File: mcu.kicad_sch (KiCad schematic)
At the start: 35 parts, among them J2 SWD, J3 SWC, U1 NRF52840-QIAA-R, Y1 ECS-.327-9-34B-TR, Y2 XRCGB32M000F1S2KR0

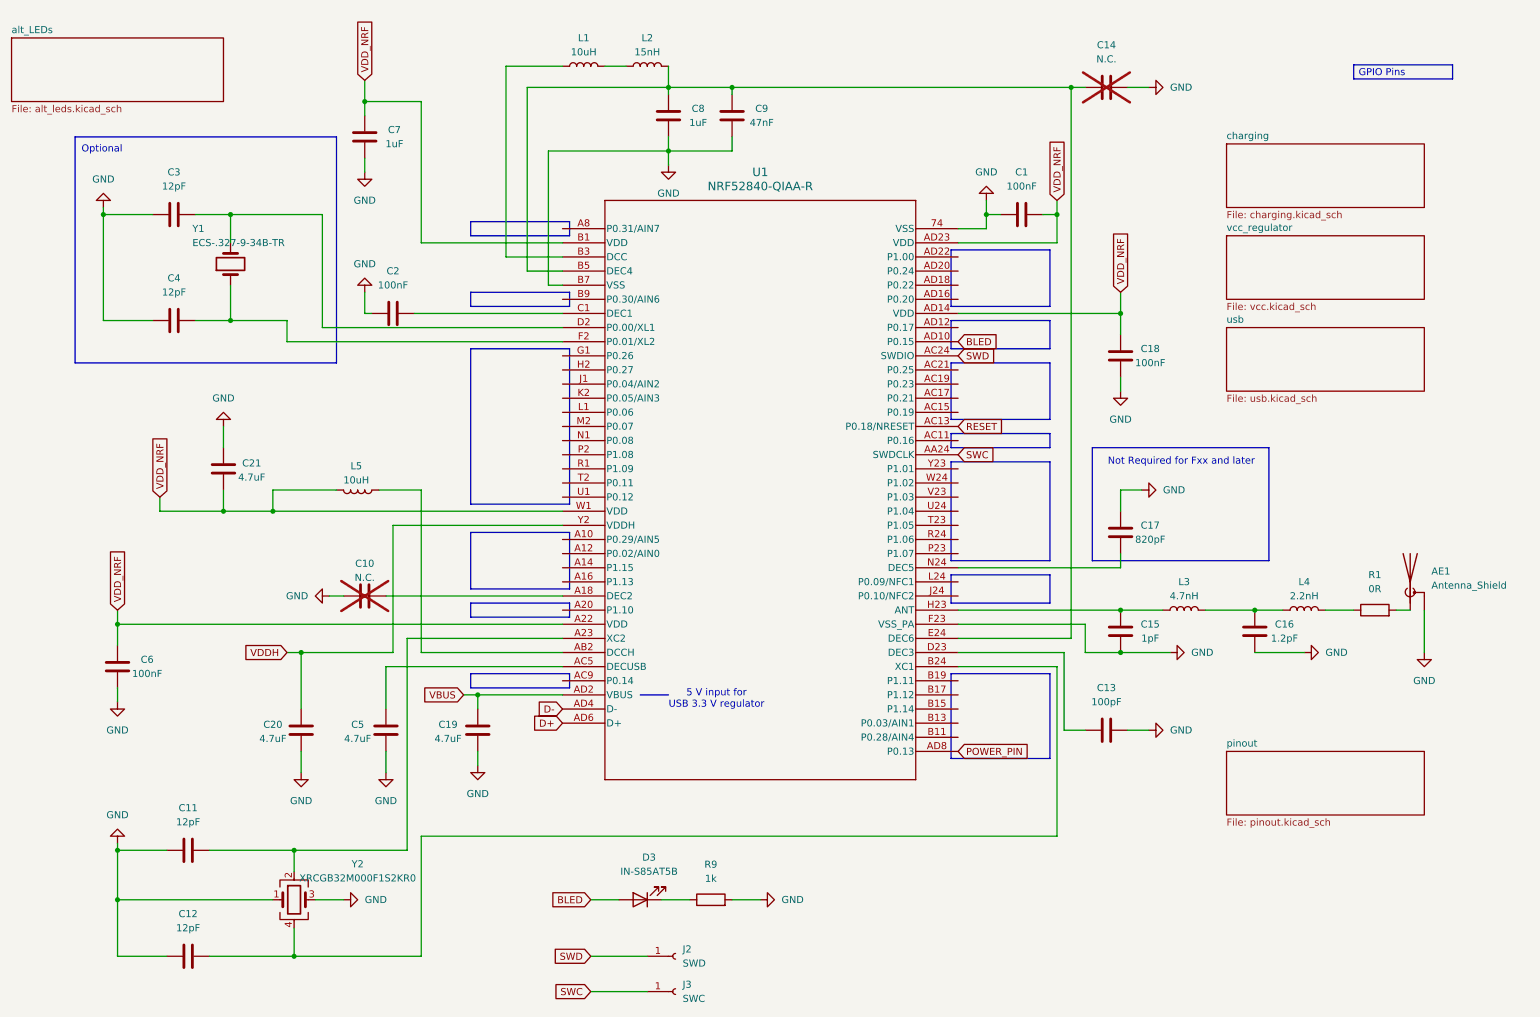
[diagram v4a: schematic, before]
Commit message: Connected GPIO
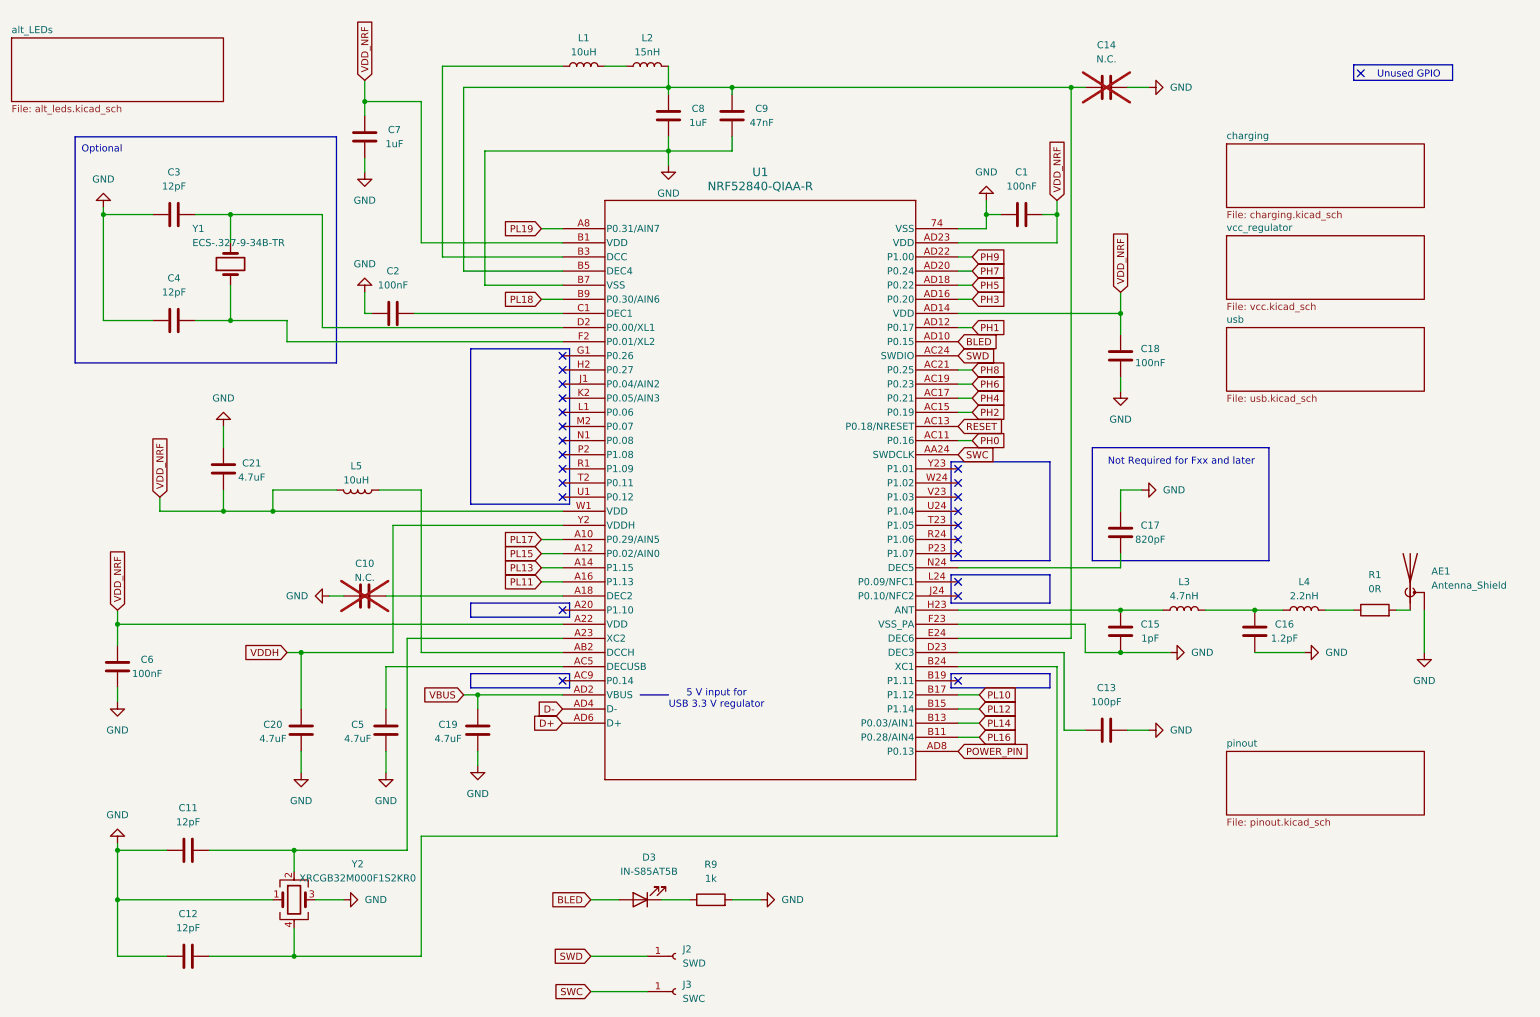
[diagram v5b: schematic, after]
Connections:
- net PL17: now reaches U1.A10 (P0.29/AIN5)
- net PL15: now reaches U1.A12 (P0.02/AIN0)
- net PL13: now reaches U1.A14 (P1.15)
- net PL11: now reaches U1.A16 (P1.13)
- net PL19: now reaches U1.A8 (P0.31/AIN7)
- net PH0: now reaches U1.AC11 (P0.16)
- net PH2: now reaches U1.AC15 (P0.19)
- net PH4: now reaches U1.AC17 (P0.21)
- net PH6: now reaches U1.AC19 (P0.23)
- net PH8: now reaches U1.AC21 (P0.25)
- net PH1: now reaches U1.AD12 (P0.17)
- net PH3: now reaches U1.AD16 (P0.20)
- net PH5: now reaches U1.AD18 (P0.22)
- net PH7: now reaches U1.AD20 (P0.24)
- net PH9: now reaches U1.AD22 (P1.00)
- net PL16: now reaches U1.B11 (P0.28/AIN4)
- net PL14: now reaches U1.B13 (P0.03/AIN1)
- net PL12: now reaches U1.B15 (P1.14)
- net PL10: now reaches U1.B17 (P1.12)
- net PL18: now reaches U1.B9 (P0.30/AIN6)
- no-connect marks 0 -> 24
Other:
- note added: "Unused GPIO"
- note removed: "GPIO Pins"

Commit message: Placed Components and started routing
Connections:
- net GND: now also Y2.2, Y2.4; no longer Y2.1, Y2.3
- net at C12.1, U1.B24 (XC1): now also Y2.1; no longer Y2.4
- net at C11.1, U1.A23 (XC2): now also Y2.3; no longer Y2.2
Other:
- moved on the sheet: Y2
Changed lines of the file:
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@@
 	)
 	(junction
-		(at 69.85 163.83)
+		(at 71.12 128.27)
 		(diameter 0)
 		(color 0 0 0 0)
@@
 	)
 	(junction
-		(at 71.12 128.27)
+		(at 38.1 163.83)
 		(diameter 0)
 		(color 0 0 0 0)
 	)
 	(junction
-		(at 38.1 163.83)
+		(at 58.42 49.53)
 		(diameter 0)
 		(color 0 0 0 0)
 	)
 	(junction
-		(at 58.42 49.53)
+		(at 57.15 102.87)
 		(diameter 0)
 		(color 0 0 0 0)
 	)
 	(junction
-		(at 38.1 172.72)
+		(at 148.59 26.67)
 		(diameter 0)
 		(color 0 0 0 0)
 	)
 	(junction
-		(at 57.15 102.87)
+		(at 38.1 172.72)
 		(diameter 0)
 		(color 0 0 0 0)
 	)
 	(junction
-		(at 148.59 26.67)
+		(at 69.85 163.83)
 		(diameter 0)
 		(color 0 0 0 0)
@@
 	(wire
 		(pts
+			(xy 69.85 163.83) (xy 69.85 168.91)
+		)
+		(stroke
+			(width 0)
+			(type default)
+		)
+	)
+	(wire
+		(pts
 			(xy 148.59 26.67) (xy 137.16 26.67)
 		)
@@
 	(wire
 		(pts
-			(xy 267.97 120.65) (xy 270.51 120.65)
+			(xy 69.85 182.88) (xy 92.71 182.88)
 		)
 		(stroke
@@
 	(wire
 		(pts
-			(xy 242.57 128.27) (xy 251.46 128.27)
+			(xy 267.97 120.65) (xy 270.51 120.65)
 		)
 		(stroke
@@
 	(wire
 		(pts
-			(xy 38.1 172.72) (xy 66.04 172.72)
+			(xy 242.57 128.27) (xy 251.46 128.27)
 		)
 		(stroke
@@
 	(wire
 		(pts
-			(xy 69.85 163.83) (xy 90.17 163.83)
+			(xy 96.52 22.86) (xy 118.11 22.86)
 		)
 		(stroke
@@
 	(wire
 		(pts
-			(xy 96.52 22.86) (xy 118.11 22.86)
+			(xy 189.23 59.69) (xy 191.77 59.69)
 		)
 		(stroke
@@
 	(wire
 		(pts
-			(xy 189.23 59.69) (xy 191.77 59.69)
+			(xy 69.85 176.53) (xy 69.85 182.88)
 		)
 		(stroke
@@
 	(wire
 		(pts
+			(xy 38.1 172.72) (xy 64.77 172.72)
+		)
+		(stroke
+			(width 0)
+			(type default)
+		)
+	)
+	(wire
+		(pts
 			(xy 38.1 163.83) (xy 38.1 162.56)
 		)
@@
 	(wire
 		(pts
+			(xy 38.1 172.72) (xy 38.1 182.88)
+		)
+		(stroke
+			(width 0)
+			(type default)
+		)
+	)
+	(wire
+		(pts
 			(xy 118.11 54.61) (xy 92.71 54.61)
 		)
@@
 	(wire
 		(pts
-			(xy 54.61 182.88) (xy 69.85 182.88)
-		)
-		(stroke
-			(width 0)
-			(type default)
-		)
-	)
-	(wire
-		(pts
 			(xy 148.59 172.72) (xy 153.67 172.72)
 		)
@@
 	(wire
 		(pts
-			(xy 38.1 172.72) (xy 38.1 182.88)
-		)
-		(stroke
-			(width 0)
-			(type default)
-		)
-	)
-	(wire
-		(pts
 			(xy 74.93 49.53) (xy 58.42 49.53)
 		)
@@
 	(wire
 		(pts
-			(xy 69.85 177.8) (xy 69.85 182.88)
-		)
-		(stroke
-			(width 0)
-			(type default)
-		)
-	)
-	(wire
-		(pts
 			(xy 74.93 69.85) (xy 74.93 49.53)
 		)
@@
 	(wire
 		(pts
+			(xy 74.93 172.72) (xy 78.74 172.72)
+		)
+		(stroke
+			(width 0)
+			(type default)
+		)
+	)
+	(wire
+		(pts
 			(xy 118.11 128.27) (xy 92.71 128.27)
 		)
@@
 	(wire
 		(pts
-			(xy 73.66 172.72) (xy 78.74 172.72)
-		)
-		(stroke
-			(width 0)
-			(type default)
-		)
-	)
-	(wire
-		(pts
 			(xy 38.1 120.65) (xy 38.1 123.19)
 		)
@@
 	(wire
 		(pts
-			(xy 69.85 163.83) (xy 69.85 167.64)
-		)
-		(stroke
-			(width 0)
-			(type default)
-		)
-	)
-	(wire
-		(pts
 			(xy 209.55 26.67) (xy 148.59 26.67)
 		)
@@
 	(wire
 		(pts
-			(xy 69.85 182.88) (xy 92.71 182.88)
+			(xy 54.61 182.88) (xy 69.85 182.88)
 		)
 		(stroke
@@
 		)
 	)
+	(wire
+		(pts
+			(xy 69.85 163.83) (xy 90.17 163.83)
+		)
+		(stroke
+			(width 0)
+			(type default)
+		)
+	)
 	(global_label "PL13"
 		(shape input)
@@
 	(symbol
 		(lib_id "Device:Crystal_GND24")
-		(at 69.85 172.72 0)
+		(at 69.85 172.72 90)
 		(unit 1)
 		(exclude_from_sim no)
@@
 		(fields_autoplaced yes)
 		(property "Reference" "Y2"
-			(at 81.28 166.2998 0)
+			(at 86.36 167.7668 90)
 			(effects
 				(font
@@
 		)
 		(property "Value" "XRCGB32M000F1S2KR0"
-			(at 81.28 168.8398 0)
+			(at 86.36 170.3068 90)
 			(effects
 				(font

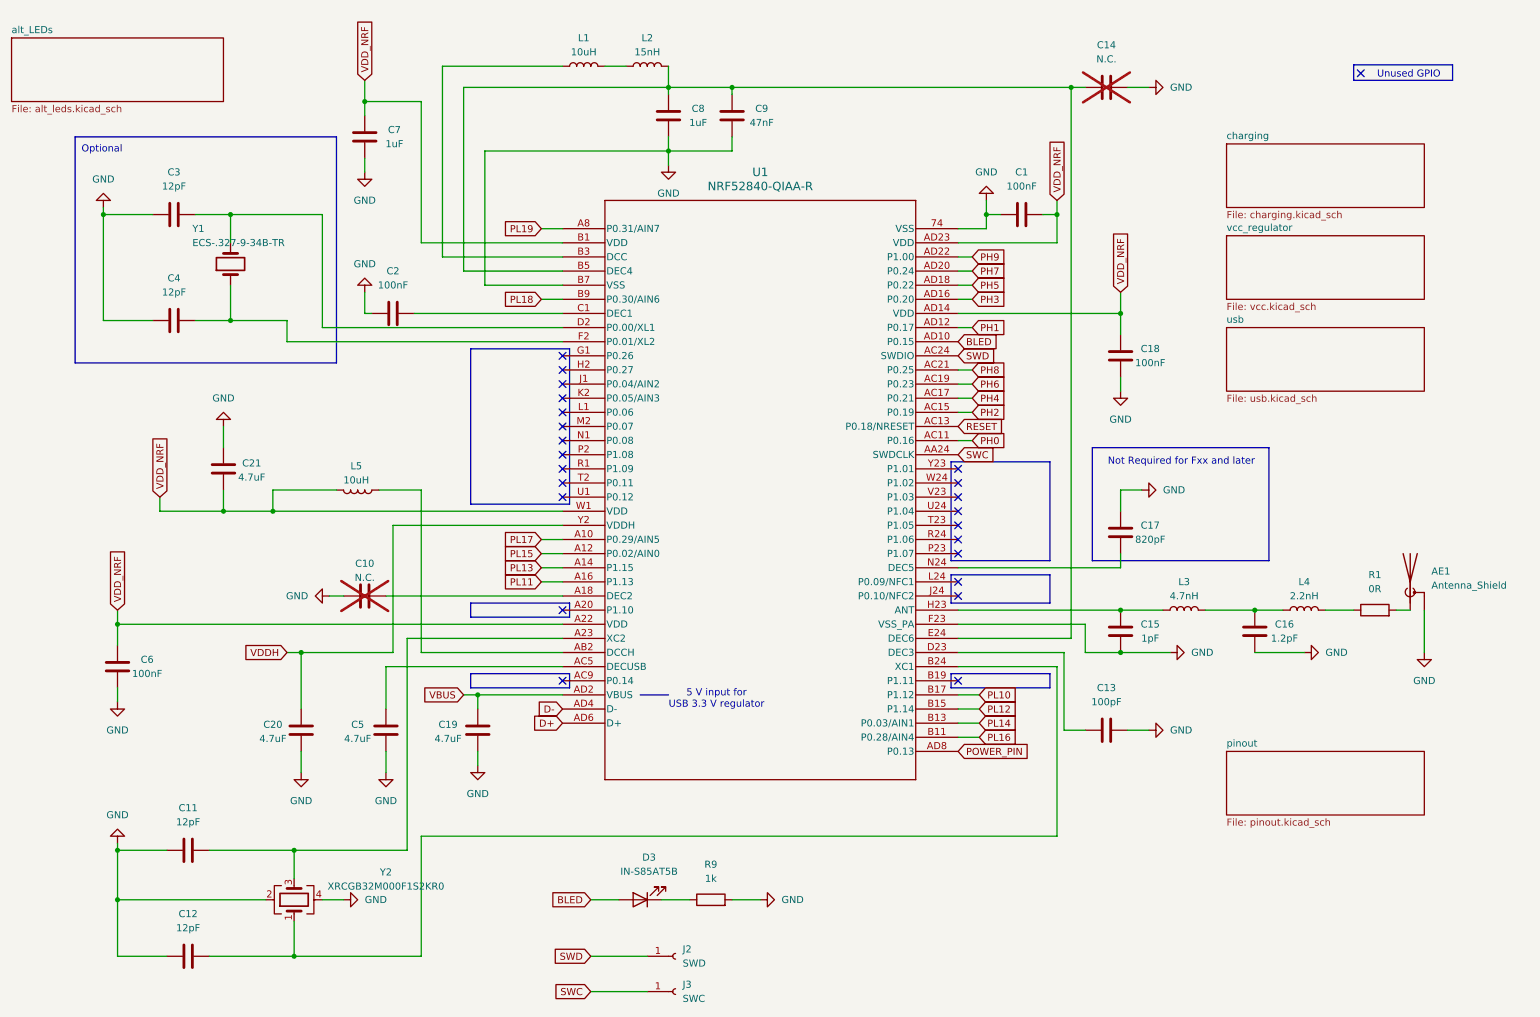
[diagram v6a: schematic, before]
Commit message: Routing Done; DFM problems to solve
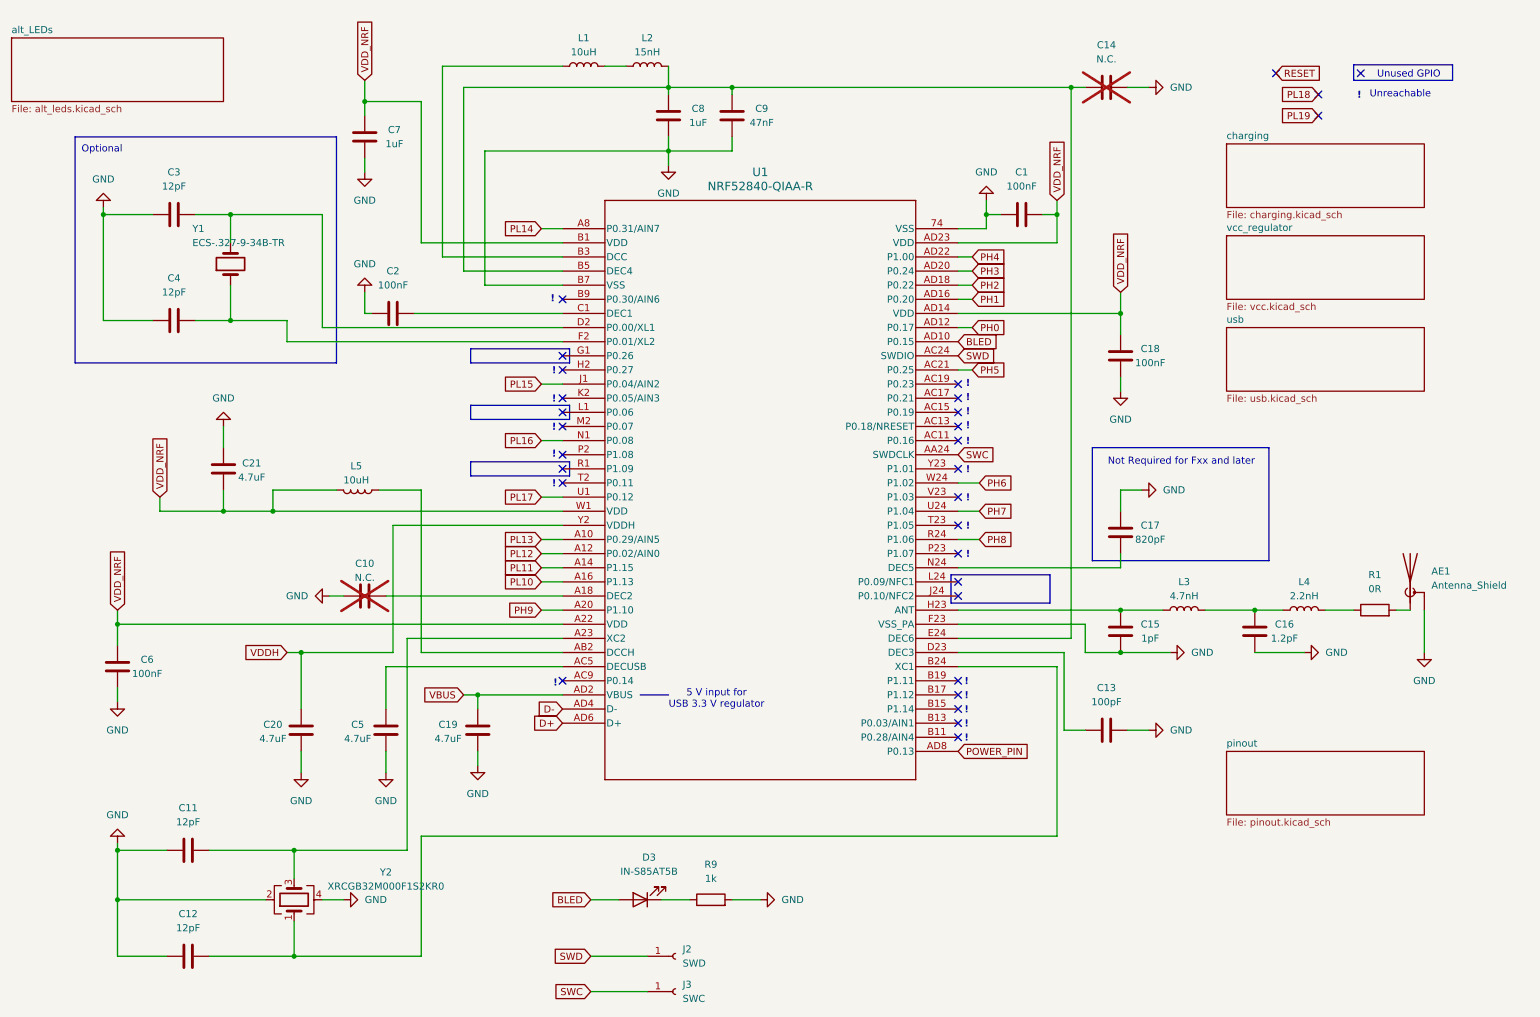
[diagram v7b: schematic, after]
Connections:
- net PH0: now also U1.AD12 (P0.17); no longer U1.AC11 (P0.16)
- net PH1: now also U1.AD16 (P0.20); no longer U1.AD12 (P0.17)
- net PH2: now also U1.AD18 (P0.22); no longer U1.AC15 (P0.19)
- net PH3: now also U1.AD20 (P0.24); no longer U1.AD16 (P0.20)
- net PH4: now also U1.AD22 (P1.00); no longer U1.AC17 (P0.21)
- net PH5: now also U1.AC21 (P0.25); no longer U1.AD18 (P0.22)
- net PH6: now also U1.W24 (P1.02); no longer U1.AC19 (P0.23)
- net PH7: now also U1.U24 (P1.04); no longer U1.AD20 (P0.24)
- net PH8: now also U1.R24 (P1.06); no longer U1.AC21 (P0.25)
- net PH9: now also U1.A20 (P1.10); no longer U1.AD22 (P1.00)
- net PL10: now also U1.A16 (P1.13); no longer U1.B17 (P1.12)
- net PL11: now also U1.A14 (P1.15); no longer U1.A16 (P1.13)
- net PL12: now also U1.A12 (P0.02/AIN0); no longer U1.B15 (P1.14)
- net PL13: now also U1.A10 (P0.29/AIN5); no longer U1.A14 (P1.15)
- net PL14: now also U1.A8 (P0.31/AIN7); no longer U1.B13 (P0.03/AIN1)
- net PL15: now also U1.J1 (P0.04/AIN2); no longer U1.A12 (P0.02/AIN0)
- net PL16: now also U1.N1 (P0.08); no longer U1.B11 (P0.28/AIN4)
- net PL17: now also U1.U1 (P0.12); no longer U1.A10 (P0.29/AIN5)
- net PL18: no longer U1.B9 (P0.30/AIN6)
- net PL19: no longer U1.A8 (P0.31/AIN7)
- net RESET: no longer U1.AC13 (P0.18/NRESET)
- no-connect marks 24 -> 30
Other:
- note added: "!"
- note added: "Unreachable"
